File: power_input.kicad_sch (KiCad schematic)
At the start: 8 parts, among them J1 DC005-T20, U1 DCDC Converter

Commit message: Rev 1.3 PCB sync + second QA pass: BOM fixes, TVS decoupling, ERC cleanup
PCB (done in KiCad, verified here):
- F8 sync applied: D2 removed; D10/D11 (SS34 SMA) and U16 (PRTR5V0U2X SOT-143)
  placed and routed; R1-R8 -> 1k, D1 -> SS54, C10 -> 25V, U11 -> ACS725 updated
  in place. Footprint-level diff confirms exactly the intended delta, nothing
  else moved. DRC 0 errors / 0 unconnected pads.

Schematic fixes from the second QA pass:
- R1-R8 had NO LCSC part number (value change had landed, part number never
  did) - they would have come back unpopulated, silently killing the switch
  inputs. Set to C14676, matching R14's existing 1K 0603 so it consolidates to
  one BOM line. NOTE: todo.md originally specified C21190 - see the discrepancy
  note there and confirm before ordering.
- TP1-TP7 set in_bom no / in_pos_files no (were 7 junk lines in the JLCPCB BOM).
- Removed 4 orphan dangling wire stubs in switch_inputs.kicad_sch.
- Converted the orphan STBY hierarchical label in motor_drivers.kicad_sch to a
  global label rather than deleting it: its wire actually carried U9 pin 19, so
  deleting dropped U9.19 off the STBY net. Converting keeps the connection and
  clears the ERC hier_label_mismatch.
- Added C40-C43 (100nF 0402, C1525) for U12-U15 VCC decoupling. The switch-input
  TVS devices currently have their nearest +3.3V_ISO bypass 18-23mm away; a
  PRTR5V0U2X shunts ESD into VCC and needs somewhere local to dump it. Still
  need PCB placement - put each within ~2mm of its device's pin 4.

Every schematic edit was validated by diffing the exported netlist before and
after; connectivity is unchanged apart from the four intended new caps.
ERC errors: 10 -> 5 (remaining are 4x missing PWR_FLAG and one J2-GND/U1-(-Vout)
both-power-output pair that is correct by design).

Added barn-blinds-controller.kicad_dru: isolation-barrier audit rule. The board
has no dedicated ISO/MOTOR gap - minimum copper spacing between domains is
0.20mm, the global default. Rev 1.2 measured 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
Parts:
- TP1, TP2: now left out of the parts list
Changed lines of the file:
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@@
 		(body_style 1)
 		(exclude_from_sim no)
-		(in_bom yes)
-		(on_board yes)
-		(in_pos_files yes)
+		(in_bom no)
+		(on_board yes)
+		(in_pos_files no)
 		(dnp no)
 		(fields_autoplaced yes)
@@
 		(body_style 1)
 		(exclude_from_sim no)
-		(in_bom yes)
-		(on_board yes)
-		(in_pos_files yes)
-		(dnp no)
-		(fields_autoplaced yes)
+		(in_bom no)
+		(on_board yes)
+		(in_pos_files no)
+		(dnp no)
+		(fields_autoplaced yes)

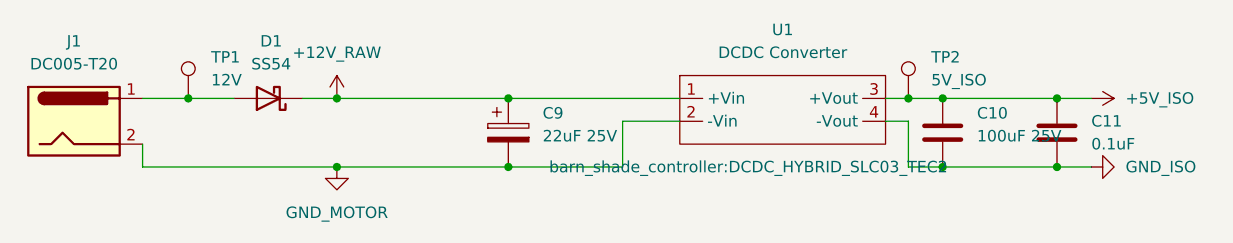
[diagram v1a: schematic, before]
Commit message: Stock-driven part swaps (C10, U12-U16) + J3 DNP after BOM audit
C10 (isolated 5V_ISO bulk cap): 100uF 25V (C2840614) was out of stock at
JLCPCB. Swapped to 100uF 16V (C7432790, HGC1210R5107M160NSVK) - same 1210
footprint, no PCB rework. 16V chosen over 10V/6.3V alternatives to keep
DC-bias derating low on the ~5V rail (unregulated B1205S-3WR2L output).

U12-U16 (PRTR5V0U2X ESD protection): C12333 was out of stock. Swapped to
C5158049 (UMW/Youtai) - same SOT-143 footprint, no PCB rework. Checked
four other "PRTR5V0U2X"-labeled LCSC listings before picking this one -
they were mismatched (unidirectional, or 14-25V standoff instead of ~5V)
despite sharing the part name; C5158049 actually matches the real
bidirectional/0.35pF/5V-7.2V spec.

Both changes verified via netlist diff (only Value/LCSC fields changed,
zero connectivity impact) and ERC (still 5 known-benign errors).

Auditing the regenerated JLCPCB assembly-order BOM turned up a separate,
pre-existing bug: J3's LCSC (C492404) is a 5-pin header (PZ254V-11-05P),
mismatched against its 7-pin footprint - a leftover from before J3 grew
from 5->7 pins for the RTS/DTR rework, where the LCSC field (and a stale
"01x05" Description) never got updated. JLCPCB's assembly matcher didn't
flag the mismatch, it silently auto-substituted a different 5-pin part.
A real 7-pin replacement isn't in stock either, and J3 is only a backup
UART flashing path (native USB on GPIO19/20 is primary) - not worth
chasing for this run, so J3 is now marked DNP. Fixed the stale "01x05"
Description text to "01x07" so the record is correct if it's ever
un-DNP'd (LCSC still needs a real 7-pin part first if that happens).

PCB: C10/U12-U16 changes synced via F8. J3's new DNP flag still needs an
F8 sync (done after the schematic edit, not yet reflected on the board).

Updated CLAUDE.md PICK UP HERE and vsp-wsc4-todo.md with full detail.
VSP-WSC-4_1.3 production files predate all three changes - needs a
Fabrication Toolkit re-run before ordering.

Co-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
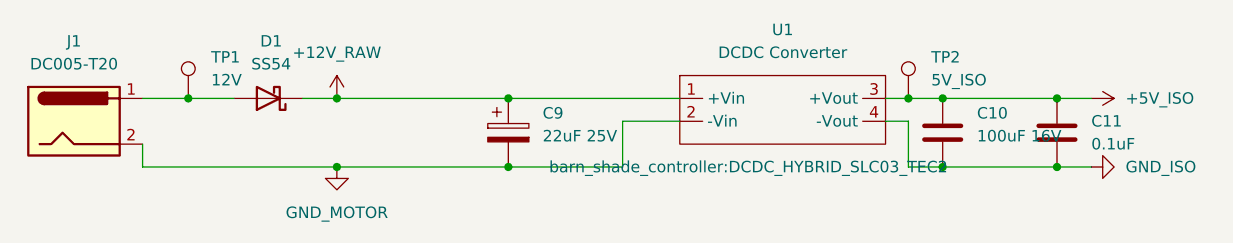
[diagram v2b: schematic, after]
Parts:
- C10: value 100uF 25V -> 100uF 16V; LCSC C2840614 -> C7432790
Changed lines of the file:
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@@
 			)
 		)
-		(property "Value" "100uF 25V"
+		(property "Value" "100uF 16V"
 			(at 176.53 79.1209 0)
 			(show_name no)
@@
 			)
 		)
-		(property "LCSC" "C2840614"
+		(property "LCSC" "C7432790"
 			(at 172.72 78.74 0)
 			(hide yes)
